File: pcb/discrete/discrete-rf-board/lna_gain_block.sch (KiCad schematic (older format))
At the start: 23 parts, among them J24 UFL, J25 UFL, Q15 BFU520R

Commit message: Autofill
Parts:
- C158, C162, C163, C164, C165, C167, C212: footprint (none) -> Capacitor_SMD:C_0402_1005Metric; Mouser (none) -> 791-RF15N101J250CT
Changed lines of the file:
@@
 F 0 "C167" V 7129 3250 50  0000 C CNN
 F 1 "100 pF RF" V 7038 3250 50  0000 C CNN
-F 2 "" H 6900 3250 50  0001 C CNN
+F 2 "Capacitor_SMD:C_0402_1005Metric" H 6900 3250 50  0001 C CNN
 F 3 "~" H 6900 3250 50  0001 C CNN
+F 4 "791-RF15N101J250CT " H 6900 3250 50  0001 C CNN "Mouser"
 	1    6900 3250
 	0    1    -1   0
@@
 F 0 "C158" V 4529 3700 50  0000 C CNN
 F 1 "100 pF RF" V 4438 3700 50  0000 C CNN
-F 2 "" H 4300 3700 50  0001 C CNN
+F 2 "Capacitor_SMD:C_0402_1005Metric" H 4300 3700 50  0001 C CNN
 F 3 "~" H 4300 3700 50  0001 C CNN
+F 4 "791-RF15N101J250CT " H 4300 3700 50  0001 C CNN "Mouser"
 	1    4300 3700
 	0    -1   -1   0
@@
 F 0 "C162" H 4810 2620 50  0000 L CNN
 F 1 "100 pF RF" H 4810 2470 50  0000 L CNN
-F 2 "" H 4800 2550 50  0001 C CNN
+F 2 "Capacitor_SMD:C_0402_1005Metric" H 4800 2550 50  0001 C CNN
 F 3 "~" H 4800 2550 50  0001 C CNN
+F 4 "791-RF15N101J250CT " H 4800 2550 50  0001 C CNN "Mouser"
 	1    4800 2550
 	1    0    0    -1
@@
 F 0 "C164" H 5210 2620 50  0000 L CNN
 F 1 "100 pF RF" H 5210 2470 50  0000 L CNN
-F 2 "" H 5200 2550 50  0001 C CNN
+F 2 "Capacitor_SMD:C_0402_1005Metric" H 5200 2550 50  0001 C CNN
 F 3 "~" H 5200 2550 50  0001 C CNN
+F 4 "791-RF15N101J250CT " H 5200 2550 50  0001 C CNN "Mouser"
 	1    5200 2550
 	1    0    0    -1
@@
 F 0 "C163" H 5160 1920 50  0000 L CNN
 F 1 "100 pF RF" H 5160 1770 50  0000 L CNN
-F 2 "" H 5150 1850 50  0001 C CNN
+F 2 "Capacitor_SMD:C_0402_1005Metric" H 5150 1850 50  0001 C CNN
 F 3 "~" H 5150 1850 50  0001 C CNN
+F 4 "791-RF15N101J250CT " H 5150 1850 50  0001 C CNN "Mouser"
 	1    5150 1850
 	1    0    0    -1
@@
 F 0 "C165" H 6192 4046 50  0000 L CNN
 F 1 "100 pF RF" H 6192 3955 50  0000 L CNN
-F 2 "" H 6100 4000 50  0001 C CNN
+F 2 "Capacitor_SMD:C_0402_1005Metric" H 6100 4000 50  0001 C CNN
 F 3 "~" H 6100 4000 50  0001 C CNN
+F 4 "791-RF15N101J250CT " H 6100 4000 50  0001 C CNN "Mouser"
 	1    6100 4000
 	1    0    0    -1
@@
 F 0 "C212" H 5742 4346 50  0000 L CNN
 F 1 "100 pF RF" H 5742 4255 50  0000 L CNN
-F 2 "" H 5650 4300 50  0001 C CNN
+F 2 "Capacitor_SMD:C_0402_1005Metric" H 5650 4300 50  0001 C CNN
 F 3 "~" H 5650 4300 50  0001 C CNN
+F 4 "791-RF15N101J250CT " H 5650 4300 50  0001 C CNN "Mouser"
 	1    5650 4300
 	1    0    0    -1

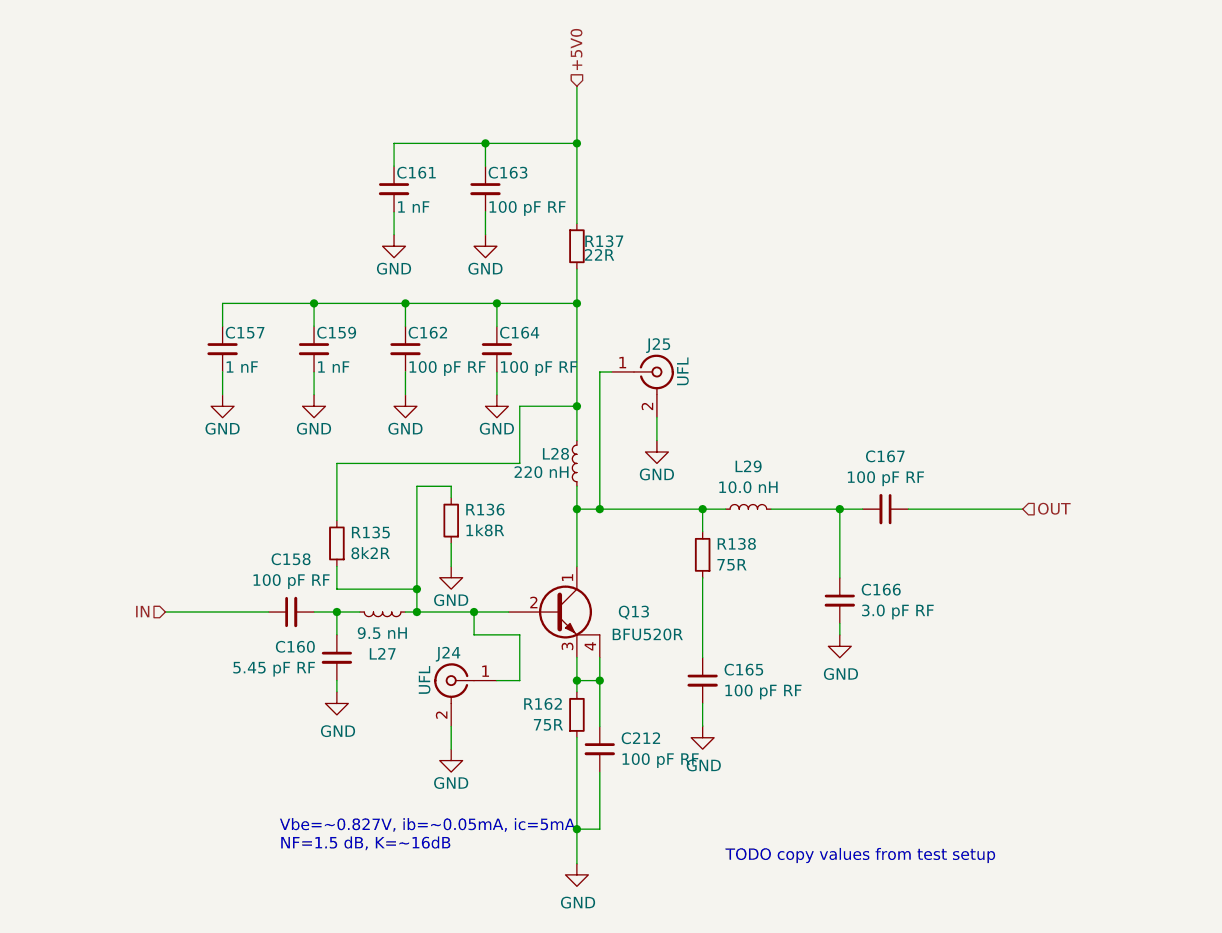
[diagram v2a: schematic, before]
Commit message: Add more footprints, saving before autofill
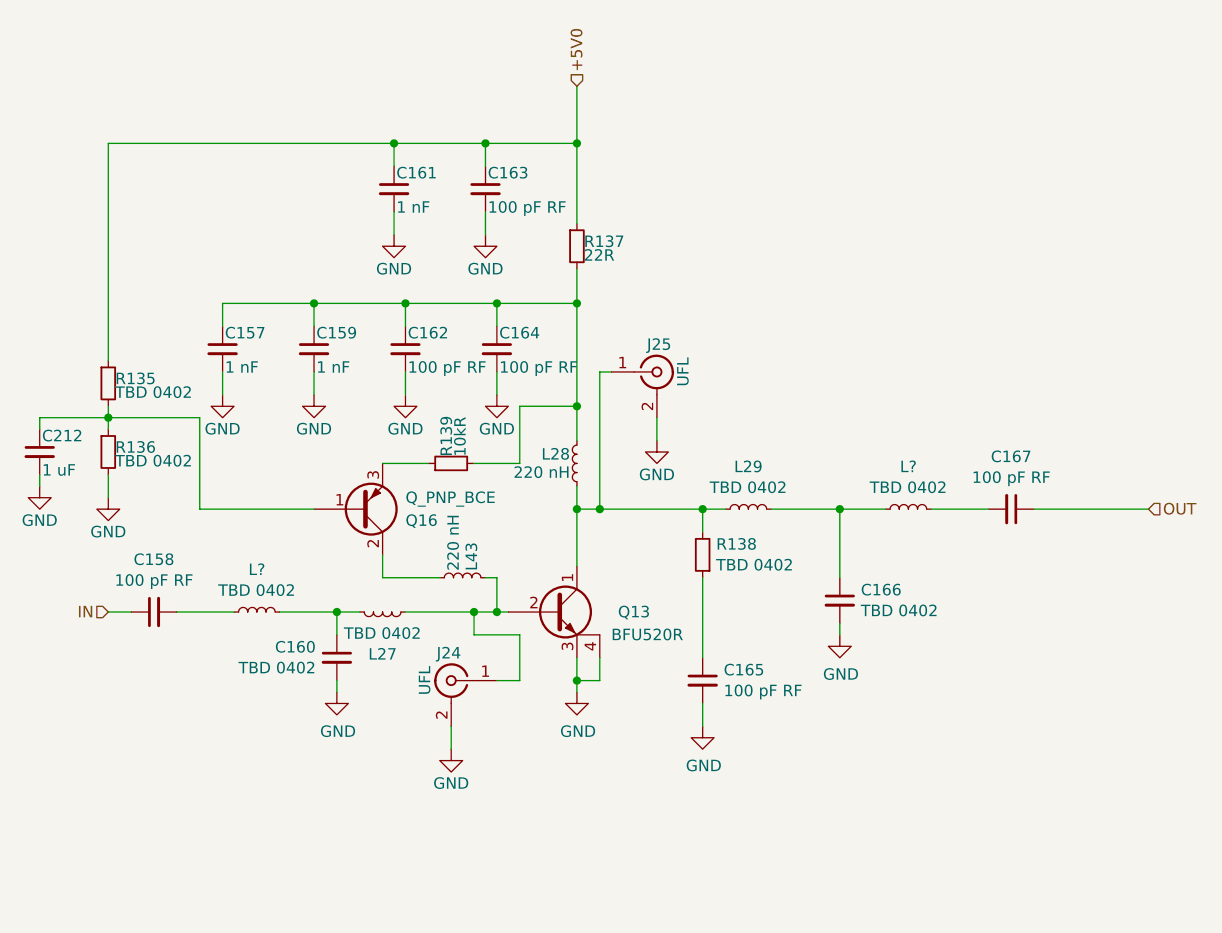
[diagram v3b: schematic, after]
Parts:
- removed R162: 75R, symbol Device:R_Small
- added L43: 220 nH, symbol Device:L_Small
- added L? (x2): TBD 0402, symbol Device:L_Small
- added Q16: Q_PNP_BCE, symbol Device:Q_PNP_BCE
- added R139: 10kR, symbol Device:R_Small
- C160: value 5.45 pF RF -> TBD 0402
- C166: value 3.0 pF RF -> TBD 0402
- C212: value 100 pF RF -> 1 uF; footprint Capacitor_SMD:C_0402_1005Metric -> (none); Mouser 791-RF15N101J250CT -> (none)
- L27: value 9.5 nH -> TBD 0402
- L29: value 10.0 nH -> TBD 0402
- R135: value 8k2R -> TBD 0402
- R136: value 1k8R -> TBD 0402
- R138: value 75R -> TBD 0402
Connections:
- net +5V0: now also R135.1
- net GND: now also Q15.3 (E), Q15.4 (C), R136.2; no longer R136.1
- net at C166.1, L29.2: now also L?.1; no longer C167.2
- net at J24.1 (In), L27.2, Q15.2 (B): now also L43.1; no longer R135.1, R136.2
- net at C157.1, C159.1, C162.1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: now also R139.2; no longer R135.2
- net at C160.1, L27.1: now also L?.1; no longer C158.2
- new net: C167.2, L?.2
- new net: C158.2, L?.2
- new net: C212.1, Q16.1 (B), R135.2, R136.1
- new net: L43.2, Q16.2 (C)
- new net: Q16.3 (E), R139.1
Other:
- note removed: "TODO copy values from test setup"
- note removed: "Vbe=~~0.827V, ib=~~0.05mA, ic=5mA\nNF=1.5 dB, K=~~16dB"
- moved on the sheet: C158, C167

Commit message: Autofill
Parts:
- C160, C166: footprint (none) -> Capacitor_SMD:C_0402_1005Metric; Mouser (none) -> 791-RF15N1R1B500CT
- R135, R136, R138: footprint (none) -> Resistor_SMD:R_0402_1005Metric; Mouser (none) -> NoPart
- R139: footprint (none) -> Resistor_SMD:R_0402_1005Metric; Mouser (none) -> 603-AC0402FR-1310KL
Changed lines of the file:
@@
 F 0 "R138" H 6041 3404 50  0000 R CNN
 F 1 "TBD 0402" H 6041 3495 50  0000 R CNN
-F 2 "" H 6100 3450 50  0001 C CNN
+F 2 "Resistor_SMD:R_0402_1005Metric" H 6100 3450 50  0001 C CNN
 F 3 "~" H 6100 3450 50  0001 C CNN
+F 4 "NoPart" H 6100 3450 50  0001 C CNN "Mouser"
 	1    6100 3450
 	-1   0    0    1
@@
 F 0 "C166" H 6792 3696 50  0000 L CNN
 F 1 "TBD 0402" H 6792 3605 50  0000 L CNN
-F 2 "" H 6700 3650 50  0001 C CNN
+F 2 "Capacitor_SMD:C_0402_1005Metric" H 6700 3650 50  0001 C CNN
 F 3 "~" H 6700 3650 50  0001 C CNN
+F 4 "791-RF15N1R1B500CT" H 6700 3650 50  0001 C CNN "Mouser"
 	1    6700 3650
 	1    0    0    -1
@@
 F 0 "C160" H 4592 3946 50  0000 L CNN
 F 1 "TBD 0402" H 4592 3855 50  0000 L CNN
-F 2 "" H 4500 3900 50  0001 C CNN
+F 2 "Capacitor_SMD:C_0402_1005Metric" H 4500 3900 50  0001 C CNN
 F 3 "~" H 4500 3900 50  0001 C CNN
+F 4 "791-RF15N1R1B500CT" H 4500 3900 50  0001 C CNN "Mouser"
 	1    4500 3900
 	-1   0    0    -1
@@
 F 0 "R139" H 5030 3070 50  0000 L CNN
 F 1 "10kR" H 5030 3010 50  0000 L CNN
-F 2 "" H 5000 3050 50  0001 C CNN
+F 2 "Resistor_SMD:R_0402_1005Metric" H 5000 3050 50  0001 C CNN
 F 3 "~" H 5000 3050 50  0001 C CNN
+F 4 "603-AC0402FR-1310KL" H 5000 3050 50  0001 C CNN "Mouser"
 	1    5000 3050
 	0    -1   -1   0
@@
 F 0 "R135" H 3530 2720 50  0000 L CNN
 F 1 "TBD 0402" H 3530 2660 50  0000 L CNN
-F 2 "" H 3500 2700 50  0001 C CNN
+F 2 "Resistor_SMD:R_0402_1005Metric" H 3500 2700 50  0001 C CNN
 F 3 "~" H 3500 2700 50  0001 C CNN
+F 4 "NoPart" H 3500 2700 50  0001 C CNN "Mouser"
 	1    3500 2700
 	1    0    0    -1
@@
 F 0 "R136" H 3530 3020 50  0000 L CNN
 F 1 "TBD 0402" H 3530 2960 50  0000 L CNN
-F 2 "" H 3500 3000 50  0001 C CNN
+F 2 "Resistor_SMD:R_0402_1005Metric" H 3500 3000 50  0001 C CNN
 F 3 "~" H 3500 3000 50  0001 C CNN
+F 4 "NoPart" H 3500 3000 50  0001 C CNN "Mouser"
 	1    3500 3000
 	1    0    0    -1

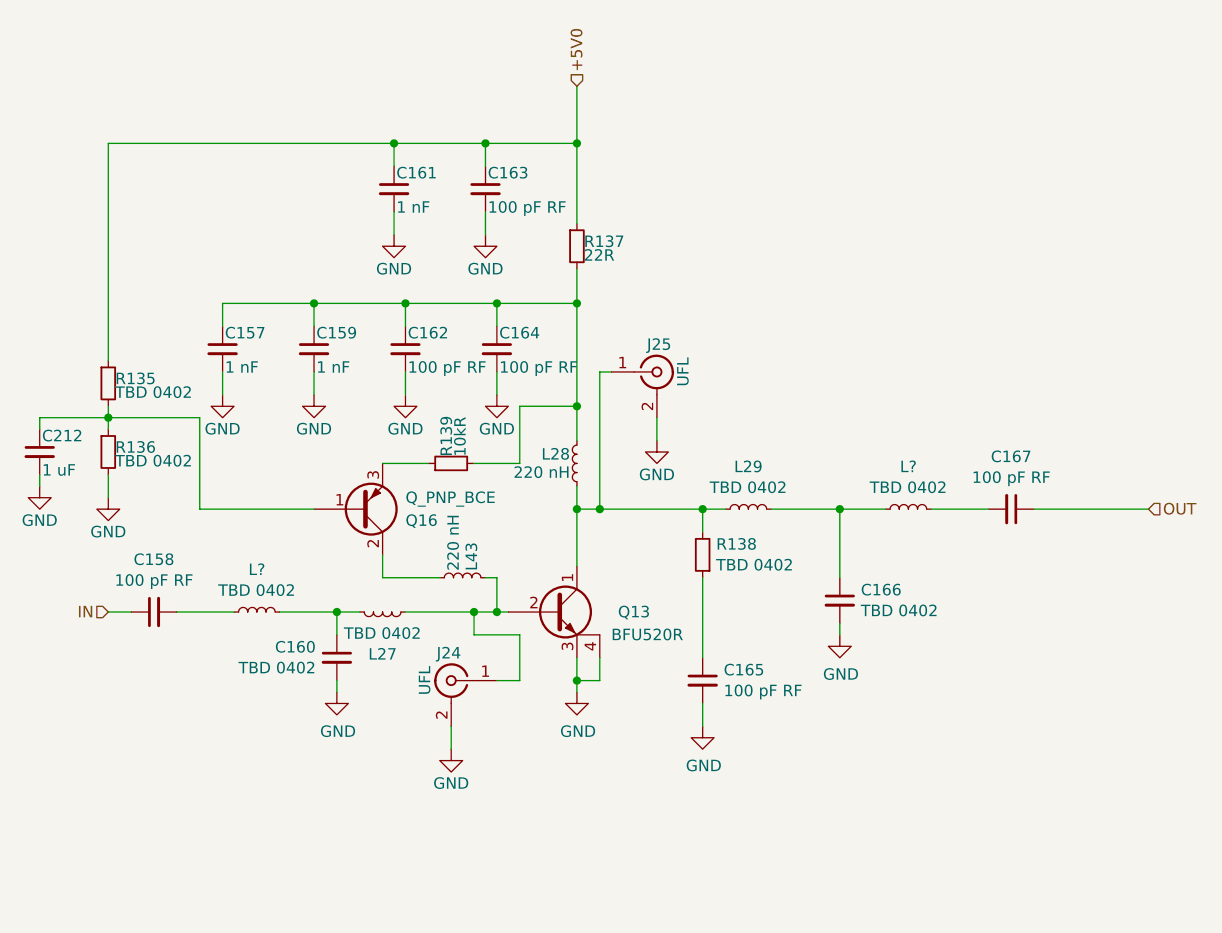
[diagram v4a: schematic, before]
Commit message: Reannotate everything; I'm trying to cut down the number of components
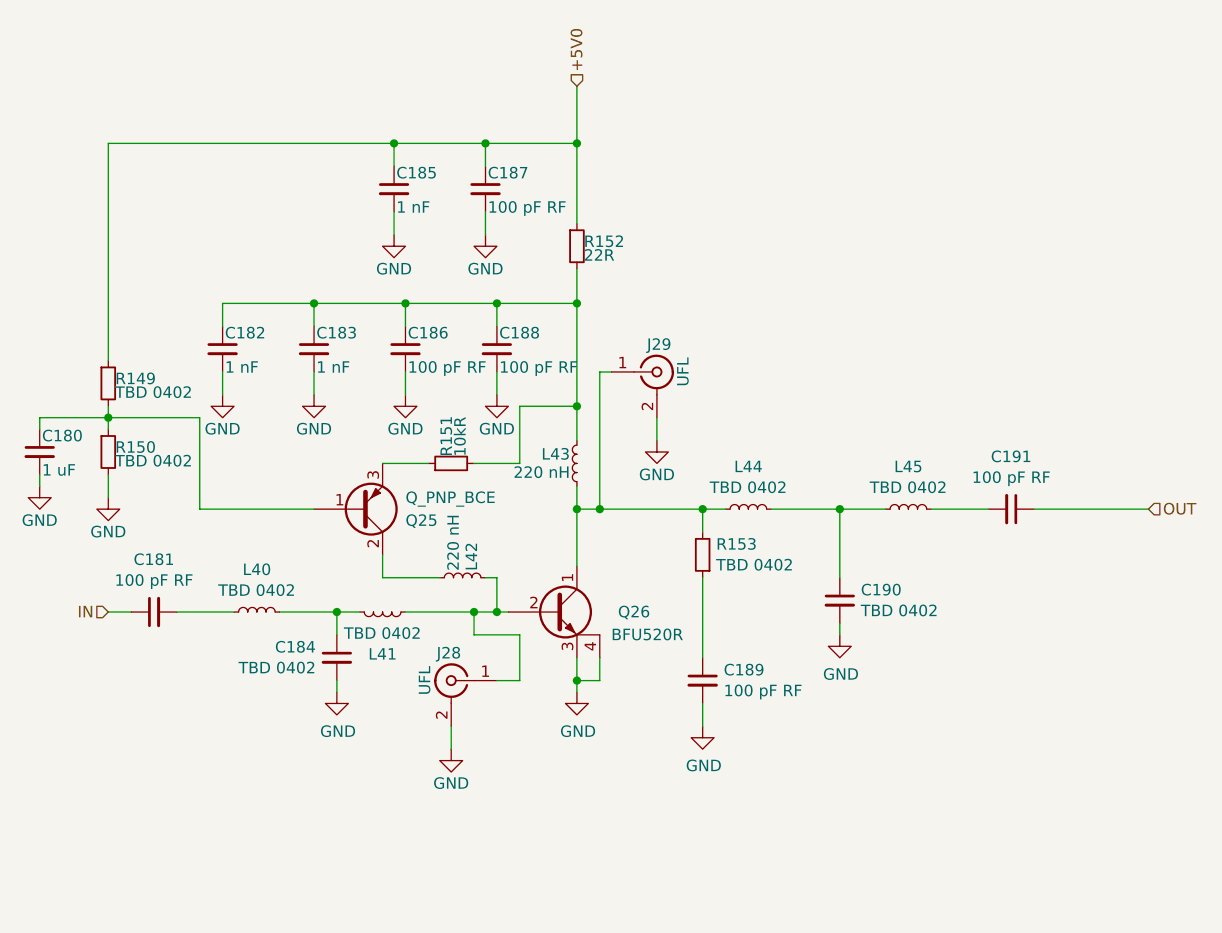
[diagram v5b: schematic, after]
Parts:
- gave numbers to parts that had none: 2
- renumbered C212 to C156, C158 to C157, C157 to C158, L27 to L29, L43 to L30, L28 to L31, L29 to L32, Q16 to Q21, Q15 to Q26, R135 to R139, R136 to R140, R139 to R141, R137 to R142, R138 to R143

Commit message: Autofill
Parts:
- C156: footprint (none) -> Capacitor_SMD:C_0402_1005Metric; Mouser (none) -> 963-EMK105BJ105KV-F
- C158, C159, C161: footprint (none) -> Capacitor_SMD:C_0402_1005Metric; Mouser (none) -> 80-C0402C102K5R7411
- L30, L31: footprint (none) -> Capacitor_SMD:C_0402_1005Metric; Mouser (none) -> 963-HK1005R22J-T
- R142: footprint (none) -> Resistor_SMD:R_0402_1005Metric; Mouser (none) -> 71-CRCW040222R0JNEDC
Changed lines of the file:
@@
 F 0 "C171" H 4410 2620 50  0000 L CNN
 F 1 "1 nF" H 4410 2470 50  0000 L CNN
-F 2 "" H 4400 2550 50  0001 C CNN
+F 2 "Capacitor_SMD:C_0402_1005Metric" H 4400 2550 50  0001 C CNN
 F 3 "~" H 4400 2550 50  0001 C CNN
+F 4 "80-C0402C102K5R7411" H 4400 2550 50  0001 C CNN "Mouser"
 	1    4400 2550
 	1    0    0    -1
@@
 F 0 "C173" H 4760 1920 50  0000 L CNN
 F 1 "1 nF" H 4760 1770 50  0000 L CNN
-F 2 "" H 4750 1850 50  0001 C CNN
+F 2 "Capacitor_SMD:C_0402_1005Metric" H 4750 1850 50  0001 C CNN
 F 3 "~" H 4750 1850 50  0001 C CNN
+F 4 "80-C0402C102K5R7411" H 4750 1850 50  0001 C CNN "Mouser"
 	1    4750 1850
 	1    0    0    -1
@@
 F 0 "R147" H 5580 2120 50  0000 L CNN
 F 1 "22R" H 5580 2060 50  0000 L CNN
-F 2 "" H 5550 2100 50  0001 C CNN
+F 2 "Resistor_SMD:R_0402_1005Metric" H 5550 2100 50  0001 C CNN
 F 3 "~" H 5550 2100 50  0001 C CNN
+F 4 "71-CRCW040222R0JNEDC" H 5550 2100 50  0001 C CNN "Mouser"
 	1    5550 2100
 	1    0    0    -1
@@
 F 0 "C170" H 4010 2620 50  0000 L CNN
 F 1 "1 nF" H 4010 2470 50  0000 L CNN
-F 2 "" H 4000 2550 50  0001 C CNN
+F 2 "Capacitor_SMD:C_0402_1005Metric" H 4000 2550 50  0001 C CNN
 F 3 "~" H 4000 2550 50  0001 C CNN
+F 4 "80-C0402C102K5R7411" H 4000 2550 50  0001 C CNN "Mouser"
 	1    4000 2550
 	1    0    0    -1
@@
 F 0 "L37" H 5580 3090 50  0000 L CNN
 F 1 "220 nH" H 5580 3010 50  0000 L CNN
-F 2 "" H 5550 3050 50  0001 C CNN
+F 2 "Capacitor_SMD:C_0402_1005Metric" H 5550 3050 50  0001 C CNN
 F 3 "~" H 5550 3050 50  0001 C CNN
+F 4 "963-HK1005R22J-T" H 5550 3050 50  0001 C CNN "Mouser"
 	1    5550 3050
 	-1   0    0    -1
@@
 F 0 "L36" H 5080 3590 50  0000 L CNN
 F 1 "220 nH" H 5080 3510 50  0000 L CNN
-F 2 "" H 5050 3550 50  0001 C CNN
+F 2 "Capacitor_SMD:C_0402_1005Metric" H 5050 3550 50  0001 C CNN
 F 3 "~" H 5050 3550 50  0001 C CNN
+F 4 "963-HK1005R22J-T" H 5050 3550 50  0001 C CNN "Mouser"
 	1    5050 3550
 	0    1    -1   0
@@
 F 0 "C168" H 3210 3070 50  0000 L CNN
 F 1 "1 uF" H 3210 2920 50  0000 L CNN
-F 2 "" H 3200 3000 50  0001 C CNN
+F 2 "Capacitor_SMD:C_0402_1005Metric" H 3200 3000 50  0001 C CNN
 F 3 "~" H 3200 3000 50  0001 C CNN
+F 4 "963-EMK105BJ105KV-F" H 3200 3000 50  0001 C CNN "Mouser"
 	1    3200 3000
 	1    0    0    -1
